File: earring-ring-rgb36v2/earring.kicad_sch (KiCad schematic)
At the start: 61 parts, among them J1 Conn_01x05, Q1 AO3401A, Q2 Q_Photo_NPN_EC, SW1 SW_Push, SW2 SW_Push, U1 GMA2718H09-F42-4P, U2 STM32L031G6Ux, Y1 Crystal

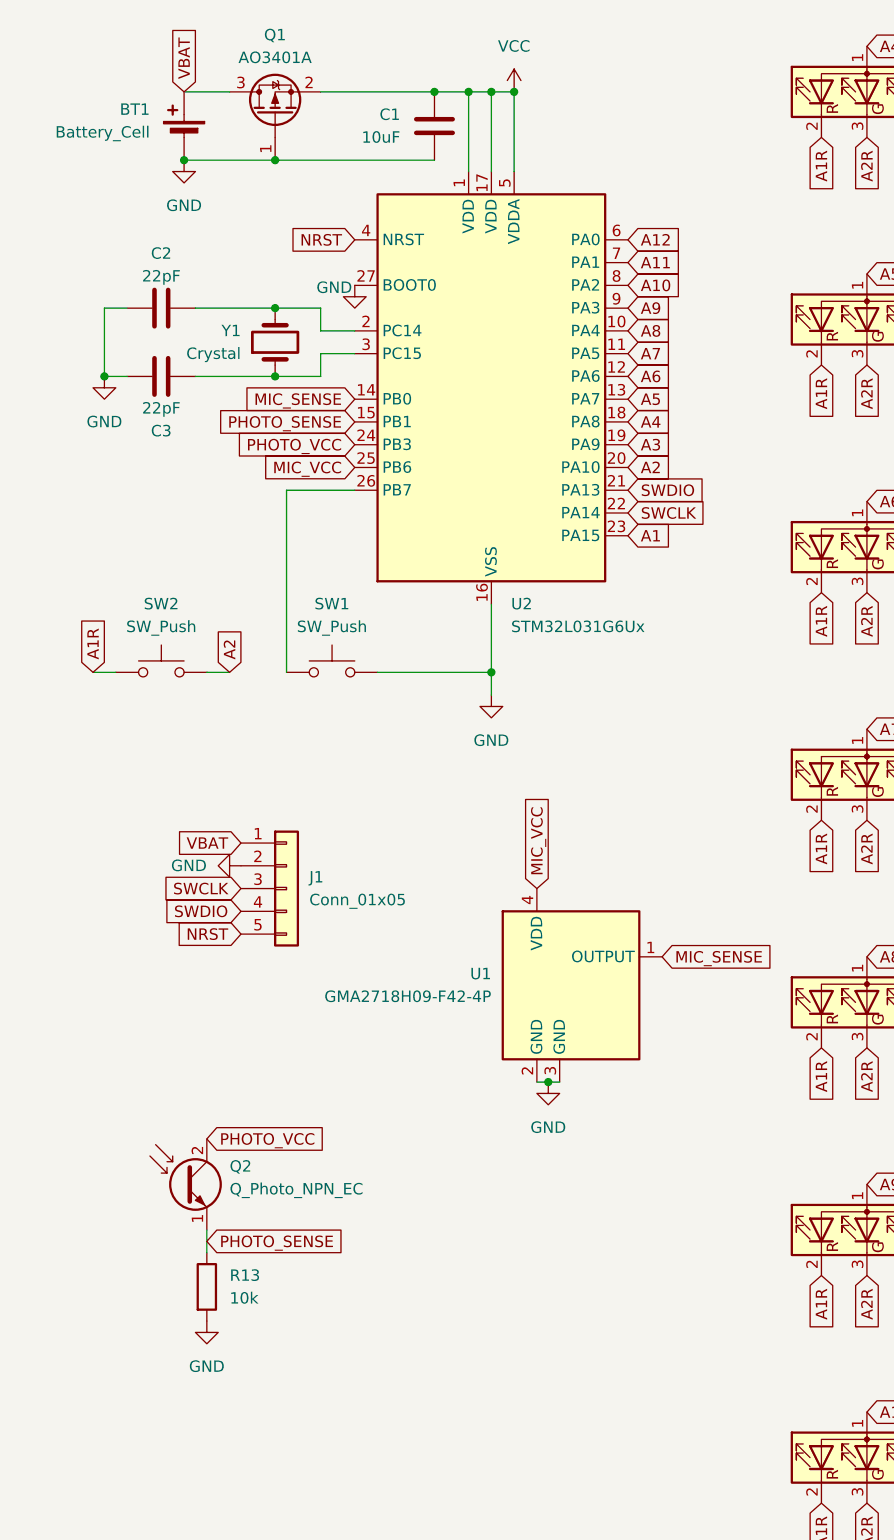
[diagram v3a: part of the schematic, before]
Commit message: earring-ring-rgb36v2: many changes for next prototype
* remove crystal
* remove light sensor
* add extra button
* add capacitor to VDDA and to the microphone
* move capacitor to above the chip
* many small changes to make the design look a bit more symmetric
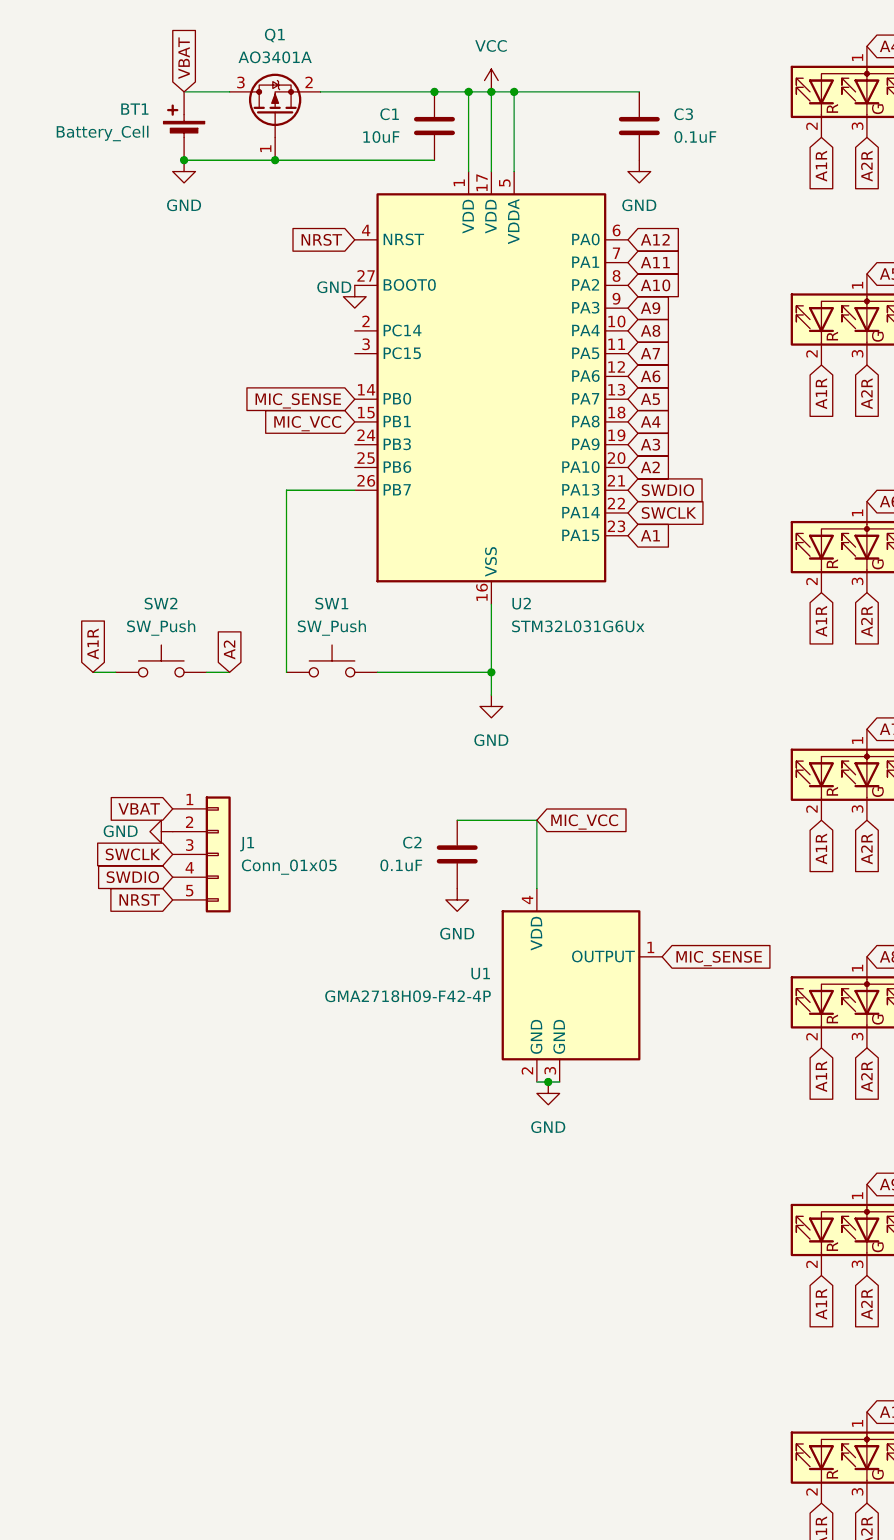
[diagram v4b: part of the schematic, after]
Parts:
- removed Q2: Q_Photo_NPN_EC, Custom:Phototransistor_0603, symbol Device:Q_Photo_NPN_EC
- removed R13: 10k, Resistor_SMD:R_0402_1005Metric, symbol Device:R
- removed Y1: Crystal, Crystal:Crystal_SMD_3215-2Pin_3.2x1.5mm, symbol Device:Crystal
- C2, C3: value 22pF -> 0.1uF; LCSC C1555 -> C1525
- SW2: footprint Custom:KXT311LHS -> Button_Switch_SMD:SW_Push_SPST_NO_Alps_SKRK
- U1: LCSC (none) -> C5142165
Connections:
- net PHOTO_SENSE is gone; now on net MIC_VCC: U2.15 (PB1)
- net GND: now also C2.2, C3.2; no longer C2.1, C3.1
- net MIC_VCC: now also C2.1; no longer U2.25 (PB6)
- net VCC: now also C3.1
- net at U2.2 (PC14): no longer C2.2
- net at U2.3 (PC15): no longer C3.2
- net PHOTO_VCC: no longer names the net of U2.24 (PB3)
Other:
- moved on the sheet: J1

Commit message: earring-ring-rgb36v6: small modifications to clean up the PCB
Should be ready for test production now.
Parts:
- SW1, SW2: footprint Button_Switch_SMD:SW_Push_SPST_NO_Alps_SKRK -> Custom:SW_Push_SPST_NO_Alps_SKRK
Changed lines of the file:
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@@
 			)
 		)
-		(property "Footprint" "Button_Switch_SMD:SW_Push_SPST_NO_Alps_SKRK"
+		(property "Footprint" "Custom:SW_Push_SPST_NO_Alps_SKRK"
 			(at 26.67 82.55 0)
 			(effects
@@
 			)
 		)
-		(property "Footprint" "Button_Switch_SMD:SW_Push_SPST_NO_Alps_SKRK"
+		(property "Footprint" "Custom:SW_Push_SPST_NO_Alps_SKRK"
 			(at 45.72 82.55 0)
 			(effects

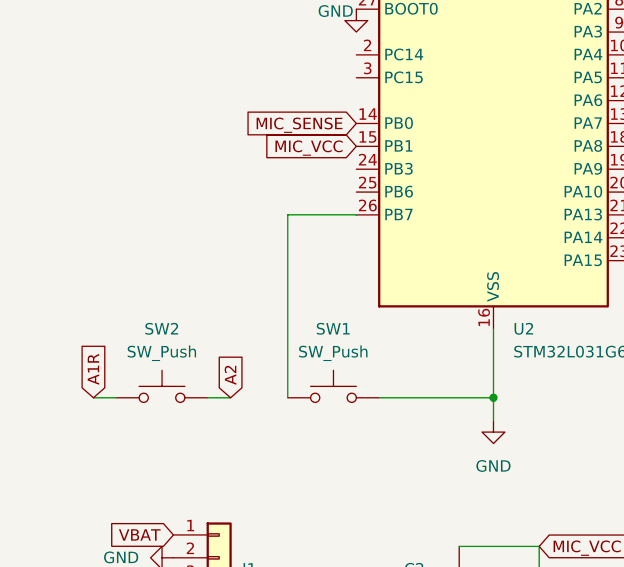
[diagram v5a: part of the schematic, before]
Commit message: earring-ring-rgb36v2: fix 2nd button wiring
Previous wiring wasn't correct: pressing the button would make some LEDs
light up that shouldn't while charlieplexing.
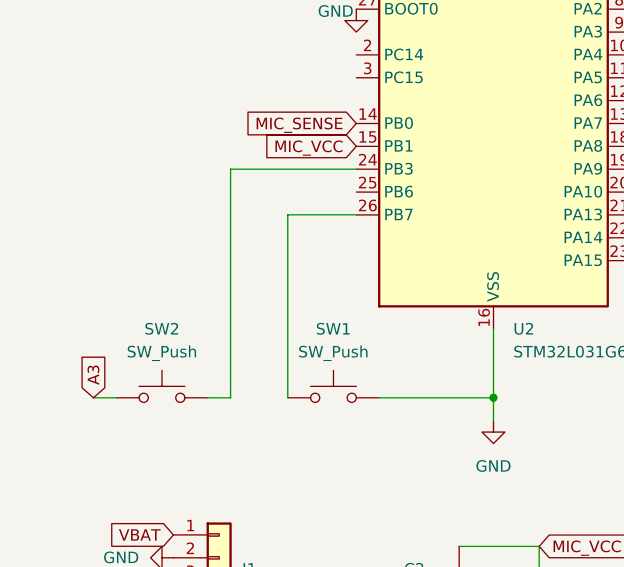
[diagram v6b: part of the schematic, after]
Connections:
- net A1R: no longer SW2.1
- net A2: no longer SW2.2
- net A3: now also SW2.1
- net at U2.24 (PB3): now also SW2.2
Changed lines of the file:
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@@
 	(wire
 		(pts
+			(xy 34.29 62.23) (xy 48.26 62.23)
+		)
+		(stroke
+			(width 0)
+			(type default)
+		)
+	)
+	(wire
+		(pts
+			(xy 34.29 87.63) (xy 34.29 62.23)
+		)
+		(stroke
+			(width 0)
+			(type default)
+		)
+	)
+	(wire
+		(pts
 			(xy 40.64 67.31) (xy 48.26 67.31)
 		)
@@
 		)
 	)
-	(global_label "A2"
-		(shape input)
-		(at 34.29 87.63 90)
-		(fields_autoplaced yes)
-		(effects
-			(font
-				(size 1.27 1.27)
-			)
-			(justify left)
-		)
-		(property "Intersheetrefs" "${INTERSHEET_REFS}"
-			(at 34.29 82.3467 90)
-			(effects
-				(font
-					(size 1.27 1.27)
-				)
-				(justify left)
-				(hide yes)
-			)
-		)
-	)
 	(global_label "A12R"
 		(shape input)
@@
 		)
 	)
-	(global_label "A1R"
+	(global_label "A3"
 		(shape input)
 		(at 19.05 87.63 90)
@@
 		)
 		(property "Intersheetrefs" "${INTERSHEET_REFS}"
-			(at 19.05 81.0767 90)
+			(at 19.05 82.3467 90)
 			(effects
 				(font

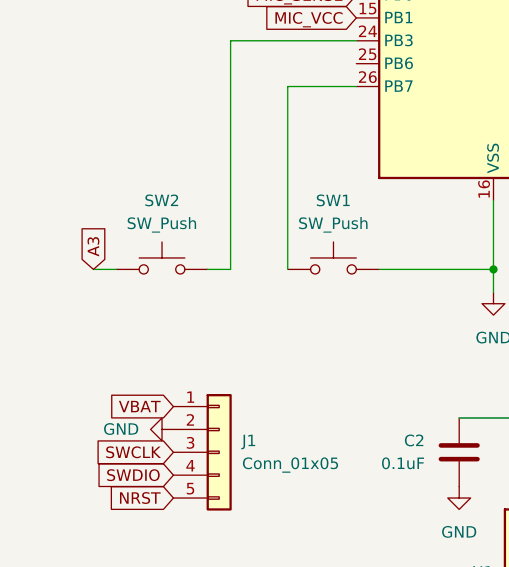
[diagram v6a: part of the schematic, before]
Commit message: earring-ring-rgb36v2: change wiring slightly to be more sensible
The button had some weird wiring, it makes much more sense to connect
the button between a pin and ground.
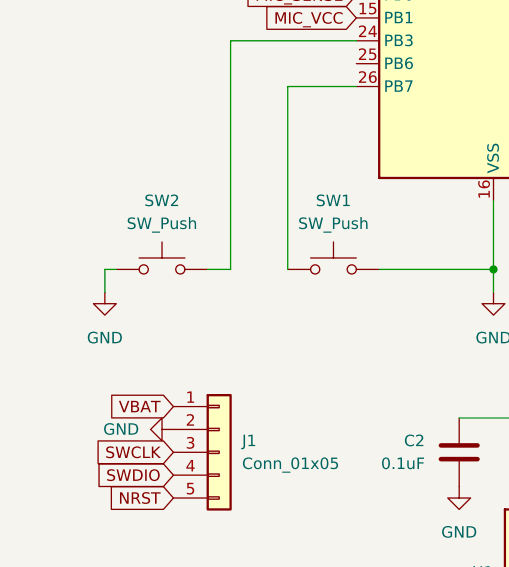
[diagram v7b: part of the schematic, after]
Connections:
- net A3: no longer SW2.1
- net GND: now also SW2.1
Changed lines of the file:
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@@
 	(wire
 		(pts
+			(xy 20.32 90.17) (xy 20.32 87.63)
+		)
+		(stroke
+			(width 0)
+			(type default)
+		)
+	)
+	(wire
+		(pts
 			(xy 63.5 87.63) (xy 63.5 90.17)
 		)
@@
 	(wire
 		(pts
-			(xy 29.21 30.48) (xy 39.37 30.48)
+			(xy 20.32 87.63) (xy 21.59 87.63)
 		)
 		(stroke
@@
 	(wire
 		(pts
-			(xy 69.85 133.35) (xy 71.12 133.35)
+			(xy 29.21 30.48) (xy 39.37 30.48)
 		)
 		(stroke
@@
 	(wire
 		(pts
-			(xy 68.58 104.14) (xy 68.58 111.76)
+			(xy 69.85 133.35) (xy 71.12 133.35)
 		)
 		(stroke
@@
 	(wire
 		(pts
-			(xy 19.05 87.63) (xy 21.59 87.63)
+			(xy 68.58 104.14) (xy 68.58 111.76)
 		)
 		(stroke
@@
 		)
 	)
-	(global_label "A3"
-		(shape input)
-		(at 19.05 87.63 90)
-		(fields_autoplaced yes)
-		(effects
-			(font
-				(size 1.27 1.27)
-			)
-			(justify left)
-		)
-		(property "Intersheetrefs" "${INTERSHEET_REFS}"
-			(at 19.05 82.3467 90)
-			(effects
-				(font
-					(size 1.27 1.27)
-				)
-				(justify left)
-				(hide yes)
-			)
-		)
-	)
 	(global_label "A12R"
 		(shape input)
@@
 		)
 		(instances
-			(project ""
+			(project "earring"
 				(path "/5b672b97-2486-4be1-9927-7141d9b63fb2"
 					(reference "R2")
@@
 		)
 		(instances
-			(project ""
+			(project "earring"
 				(path "/5b672b97-2486-4be1-9927-7141d9b63fb2"
 					(reference "R5")
@@
 		)
 		(instances
-			(project ""
+			(project "earring"
 				(path "/5b672b97-2486-4be1-9927-7141d9b63fb2"
 					(reference "R3")
@@
 		)
 		(instances
-			(project ""
+			(project "earring"
 				(path "/5b672b97-2486-4be1-9927-7141d9b63fb2"
 					(reference "R6")
@@
 		)
 		(instances
-			(project ""
+			(project "earring"
 				(path "/5b672b97-2486-4be1-9927-7141d9b63fb2"
 					(reference "Q1")
@@
 	(symbol
 		(lib_id "power:GND")
+		(at 20.32 90.17 0)
+		(unit 1)
+		(exclude_from_sim no)
+		(in_bom yes)
+		(on_board yes)
+		(dnp no)
+		(fields_autoplaced yes)
+		(property "Reference" "#PWR07"
+			(at 20.32 96.52 0)
+			(effects
+				(font
+					(size 1.27 1.27)
+				)
+				(hide yes)
+			)
+		)
+		(property "Value" "GND"
+			(at 20.32 95.25 0)
+			(effects
+				(font
+					(size 1.27 1.27)
+				)
+			)
+		)
+		(property "Footprint" ""
+			(at 20.32 90.17 0)
+			(effects
+				(font
+					(size 1.27 1.27)
+				)
+				(hide yes)
+			)
+		)
+		(property "Datasheet" ""
+			(at 20.32 90.17 0)
+			(effects
+				(font
+					(size 1.27 1.27)
+				)
+				(hide yes)
+			)
+		)
+		(property "Description" "Power symbol creates a global label with name \"GND\" , ground"
+			(at 20.32 90.17 0)
+			(effects
+				(font
+					(size 1.27 1.27)
+				)
+				(hide yes)
+			)
+		)
+		(pin "1"
+		)
+		(instances
+			(project "earring"
+				(path "/5b672b97-2486-4be1-9927-7141d9b63fb2"
+					(reference "#PWR07")
+					(unit 1)
+				)
+			)
+		)
+	)
+	(symbol
+		(lib_id "power:GND")
 		(at 29.21 30.48 0)
 		(unit 1)
@@
 		)
 		(instances
-			(project ""
+			(project "earring"
 				(path "/5b672b97-2486-4be1-9927-7141d9b63fb2"
 					(reference "#PWR09")
@@
 		)
 		(instances
-			(project ""
+			(project "earring"
 				(path "/5b672b97-2486-4be1-9927-7141d9b63fb2"
 					(reference "#PWR05")
@@
 		)
 		(instances
-			(project ""
+			(project "earring"
 				(path "/5b672b97-2486-4be1-9927-7141d9b63fb2"
 					(reference "#PWR04")
@@
 		)
 		(instances
-			(project ""
+			(project "earring"
 				(path "/5b672b97-2486-4be1-9927-7141d9b63fb2"
 					(reference "R9")
@@
 		)
 		(instances
-			(project ""
+			(project "earring"
 				(path "/5b672b97-2486-4be1-9927-7141d9b63fb2"
 					(reference "R7")
@@
 		)
 		(instances
-			(project ""
+			(project "earring"
 				(path "/5b672b97-2486-4be1-9927-7141d9b63fb2"
 					(reference "D1")
@@
 		)
 		(instances
-			(project ""
+			(project "earring"
 				(path "/5b672b97-2486-4be1-9927-7141d9b63fb2"
 					(reference "U2")
@@
 		)
 		(instances
-			(project ""
+			(project "earring"
 				(path "/5b672b97-2486-4be1-9927-7141d9b63fb2"
 					(reference "J1")
@@
 		)
 		(instances
-			(project ""
+			(project "earring"
 				(path "/5b672b97-2486-4be1-9927-7141d9b63fb2"
 					(reference "R4")
@@
 		)
 		(instances
-			(project ""
+			(project "earring"
 				(path "/5b672b97-2486-4be1-9927-7141d9b63fb2"
 					(reference "U1")
@@
 		)
 		(instances
-			(project ""
+			(project "earring"
 				(path "/5b672b97-2486-4be1-9927-7141d9b63fb2"
 					(reference "R8")
@@
 		)
 		(instances
-			(project ""
+			(project "earring"
 				(path "/5b672b97-2486-4be1-9927-7141d9b63fb2"
 					(reference "R1")

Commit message: earring-ring-rgb36v2: some more fixes before prototype production
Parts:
- SW2: LCSC (none) -> C561519
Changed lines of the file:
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@@
+			)
+		)
+		(property "LCSC" "C561519"
+			(at 26.67 87.63 0)
+			(effects
+				(font
+					(size 1.27 1.27)
+				)
+				(hide yes)
 			)
 		)
